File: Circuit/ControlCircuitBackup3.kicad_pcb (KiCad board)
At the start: 2 copper layers, 115.6 x 115.6 mm, 116 parts, among them CON501 AVR-ISP-10, IC501 ATMEGA644-A, K201 Meisei-m4-24h, K202 Meisei-m4-24h, K203 Meisei-m4-24h, K204 Meisei-m4-24h, K205 Meisei-m4-24h, K206 Meisei-m4-24h, K207 Meisei-m4-24h, K208 Meisei-m4-24h, P101 CONN_01X08, P102 CONN_01X08, P103 CONN_01X08, P104 CONN_01X08, P105 CONN_01X08, P106 CONN_01X08, P107 CONN_01X02, Q201 Q_NPN_BCE, Q202 Q_NPN_BCE, Q203 Q_NPN_BCE, Q204 Q_NPN_BCE, Q205 Q_NPN_BCE, Q206 Q_NPN_BCE, Q207 Q_NPN_BCE, Q208 Q_NPN_BCE, U301 LTV-817, U302 LTV-817, U303 LTV-817, U304 LTV-817, U305 LTV-817, U306 LTV-817, U307 LTV-817, U308 LTV-817, Y501 Crystal

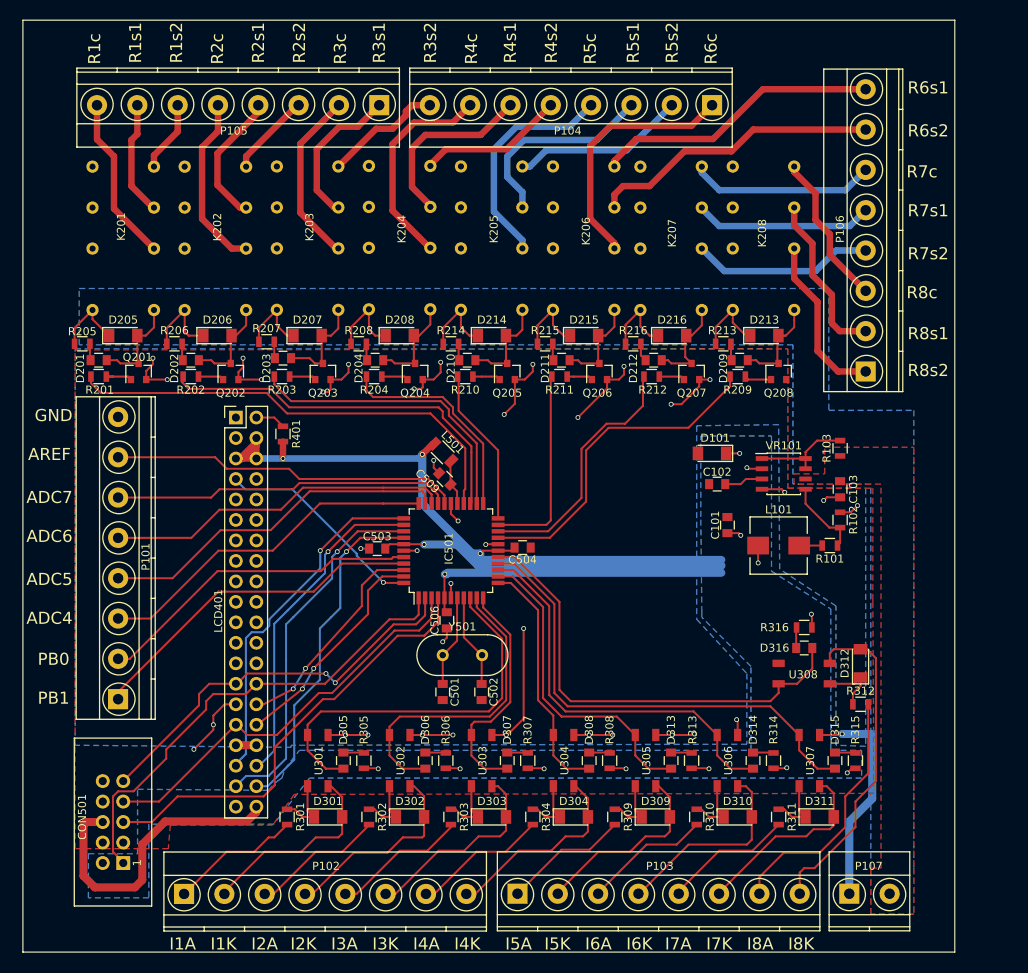
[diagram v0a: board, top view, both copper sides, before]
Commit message: Cleaned up silkscreen. Everything connected.
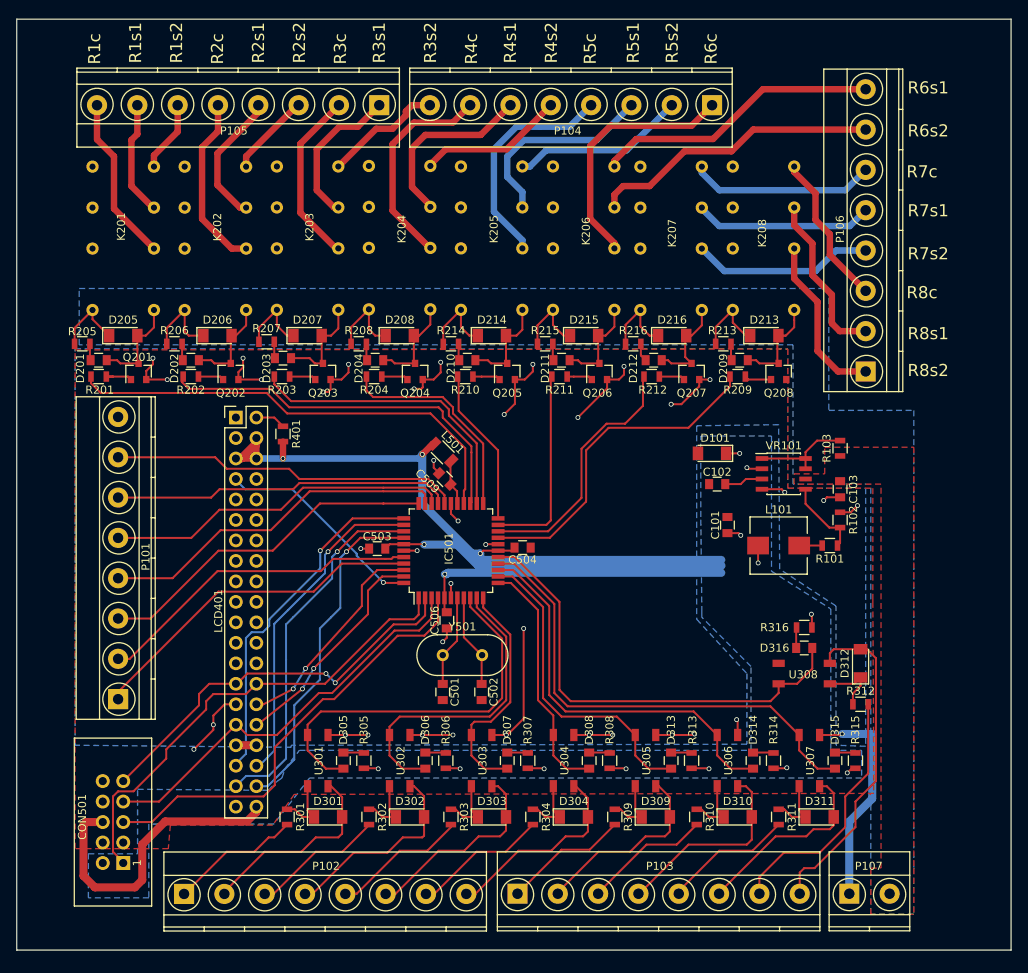
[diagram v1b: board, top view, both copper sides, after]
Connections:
- net /Microcontroller/AREF renamed /AREF
- P101 pad 8: GND -> /AVCC
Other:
- board size 115.6 x 115.6 mm -> 123.3 x 115.4 mm
- board text removed: "ADC4"
- board text removed: "ADC5"
- board text removed: "ADC6"
- board text removed: "ADC7"
- board text removed: "AREF"
- board text removed: "GND"
- board text removed: "I1A"
- board text removed: "I1K"
- board text removed: "I2A"
- board text removed: "I2K"
- board text removed: "I3A"
- board text removed: "I3K"
- board text removed: "I4A"
- board text removed: "I4K"
- board text removed: "I5A"
- board text removed: "I5K"
- board text removed: "I6A"
- board text removed: "I6K"
- board text removed: "I7A"
- board text removed: "I7K"
- board text removed: "I8A"
- board text removed: "I8K"
- board text removed: "PB0"
- board text removed: "PB1"
